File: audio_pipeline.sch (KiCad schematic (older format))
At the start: 8 parts, among them P1 CONN_4, P2 CONN_4, P3 CONN_4, P4 CONN_4, P5 CONN_4, U5 MAX4582, U6 DS1882, U8 RC4580

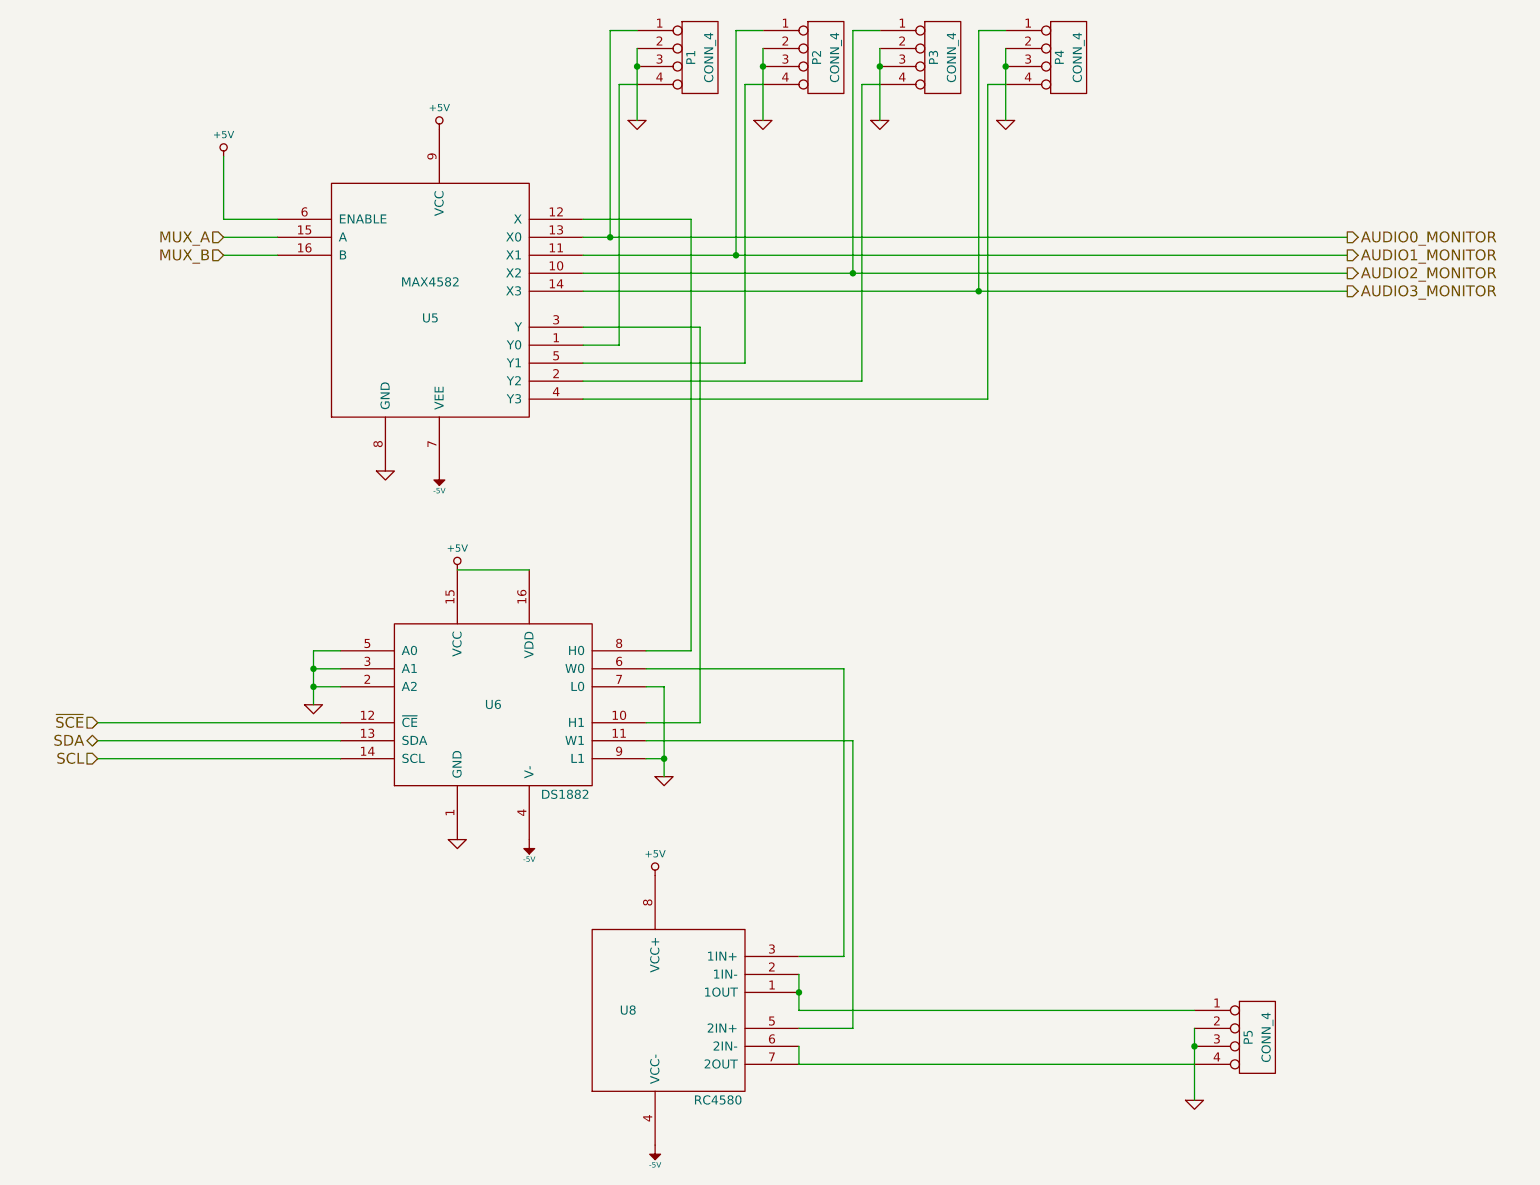
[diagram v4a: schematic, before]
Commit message: Moving back to atmega168, for cost and size reduction, new smaller board layout.
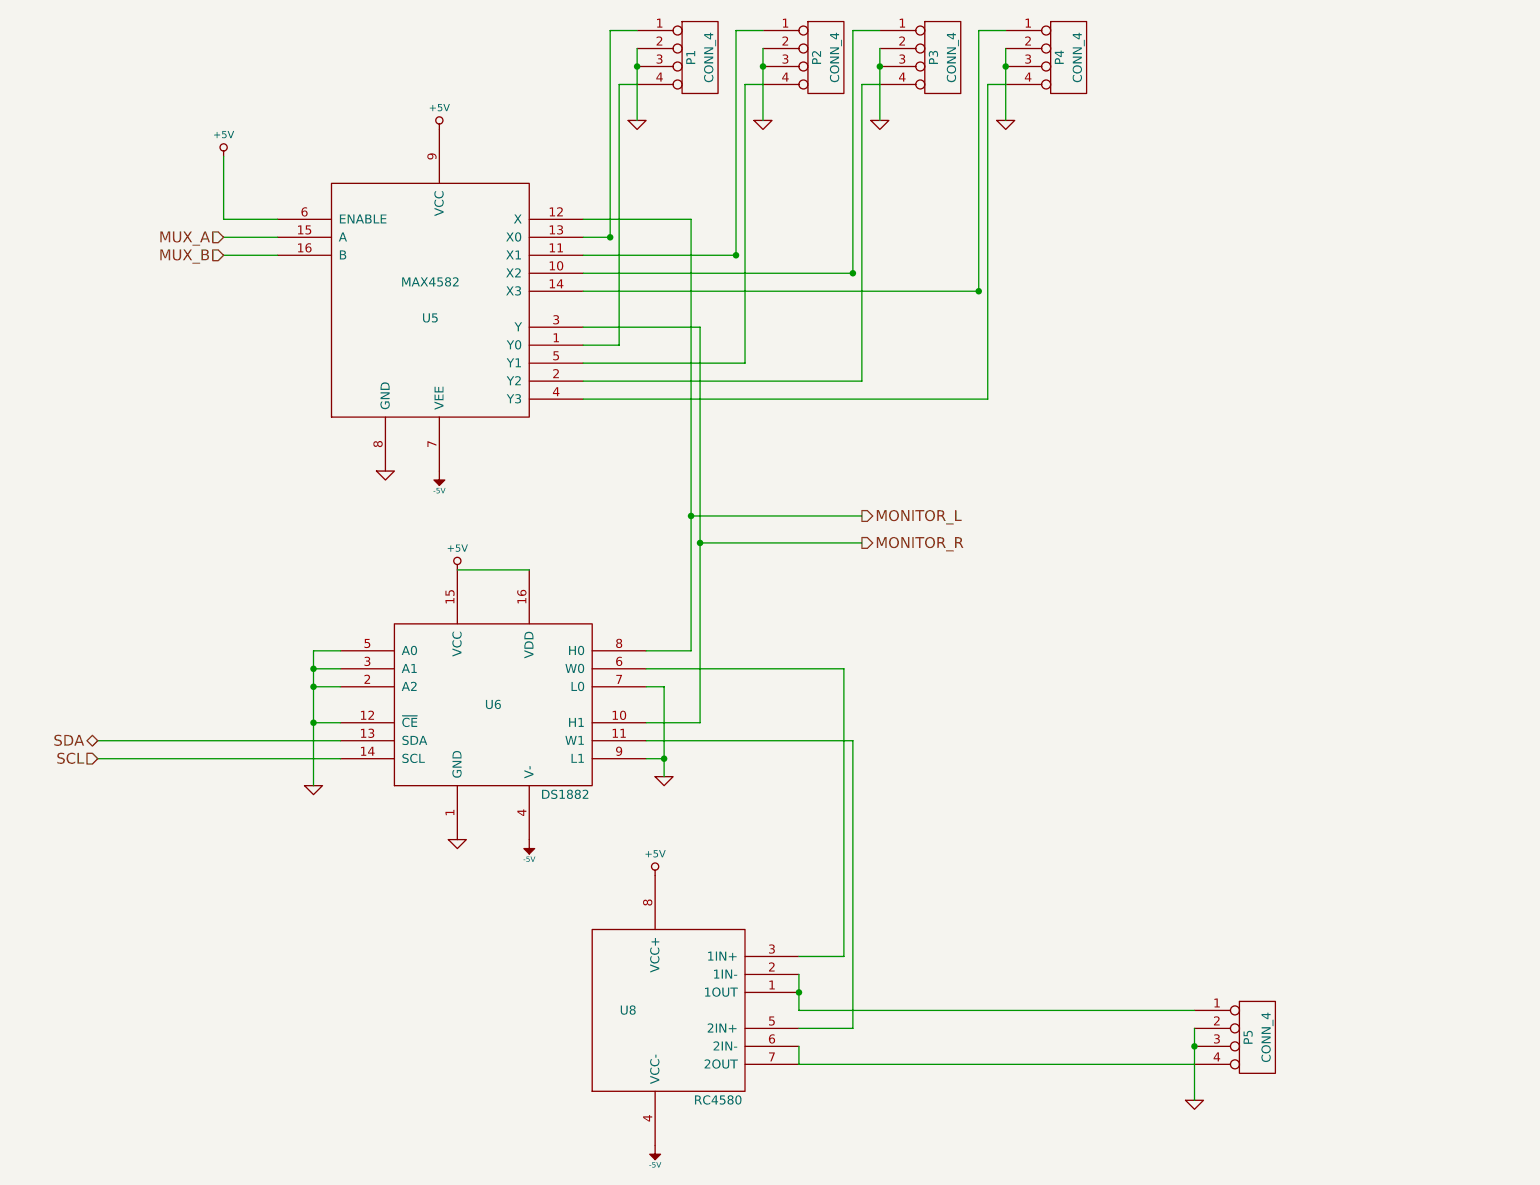
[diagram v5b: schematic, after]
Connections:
- net ~SCE is gone; now on net GND: U6.12 (~CE)
- net MONITOR_L: now reaches U5.12 (X), U6.8 (H0)
- net MONITOR_R: now reaches U5.3 (Y), U6.10 (H1)
- net AUDIO0_MONITOR: no longer names the net of P1.1 (P1), U5.13 (X0)
- net AUDIO1_MONITOR: no longer names the net of P2.1 (P1), U5.11 (X1)
- net AUDIO2_MONITOR: no longer names the net of P3.1 (P1), U5.10 (X2)
- net AUDIO3_MONITOR: no longer names the net of P4.1 (P1), U5.14 (X3)
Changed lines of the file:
@@
-EESchema Schematic File Version 2  date 7/31/2012 11:17:11 PM
+EESchema Schematic File Version 2  date 8/1/2012 10:20:13 AM
 LIBS:atmel
 LIBS:device
@@
 Comment4 ""
 $EndDescr
-Wire Wire Line
-	8400 2300 4150 2300
-Wire Wire Line
-	4150 2100 8400 2100
+Connection ~ 2650 4700
+Wire Wire Line
+	2800 4700 2650 4700
+Connection ~ 4800 3700
+Wire Wire Line
+	5700 3700 4800 3700
+Wire Wire Line
+	4150 2300 6350 2300
+Wire Wire Line
+	4150 2100 5000 2100
 Wire Wire Line
 	5350 6000 5600 6000
@@
 Connection ~ 4300 2000
 Wire Wire Line
-	4300 2000 4300 850
+	4300 850  4300 2000
 Wire Wire Line
 	4300 850  4450 850
@@
 	2800 4300 2650 4300
 Wire Wire Line
-	2650 4300 2650 4600
-Wire Wire Line
 	2800 4500 2650 4500
 Connection ~ 2650 4500
@@
 	2450 2000 2150 2000
 Wire Wire Line
-	2800 4700 1450 4700
-Wire Wire Line
 	4450 1150 4350 1150
 Wire Wire Line
@@
 	5650 6400 5350 6400
 Wire Wire Line
-	8400 2000 4150 2000
-Wire Wire Line
-	8400 2200 4150 2200
+	4300 2000 4150 2000
+Wire Wire Line
+	5650 2200 4150 2200
+Wire Wire Line
+	5700 3550 4750 3550
+Connection ~ 4750 3550
+Wire Wire Line
+	2650 4300 2650 5050
+Text HLabel 5700 3700 2    60   Output ~ 0
+MONITOR_R
+Text HLabel 5700 3550 2    60   Output ~ 0
+MONITOR_L
 $Comp
 L -5V #PWR024
@@
 	1    0    0    -1
 $EndComp
-Text HLabel 1450 4700 0    60   Input ~ 0
-~SCE
-Text HLabel 8400 2000 2    60   Output ~ 0
-AUDIO0_MONITOR
-Text HLabel 8400 2100 2    60   Output ~ 0
-AUDIO1_MONITOR
-Text HLabel 8400 2200 2    60   Output ~ 0
-AUDIO2_MONITOR
-Text HLabel 8400 2300 2    60   Output ~ 0
-AUDIO3_MONITOR
 $Comp
 L GND #PWR031
@@
 L GND #PWR035
 U 1 1 4F8E0C00
-P 2650 4600
-F 0 "#PWR035" H 2650 4600 30  0001 C CNN
-F 1 "GND" H 2650 4530 30  0001 C CNN
-	1    2650 4600
-	1    0    0    -1
-$EndComp
+P 2650 5050
+F 0 "#PWR035" H 2650 5050 30  0001 C CNN
+F 1 "GND" H 2650 4980 30  0001 C CNN
+	1    2650 5050
+	1    0    0    -1
+$EndComp

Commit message: Final board as sent for fab.
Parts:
- added C4, C6, C7, C8, C9: 0.1u, symbol C
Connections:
- net +5V: now also C4.1, C6.1, C8.1
- net -5V: now also C7.2, C9.2
- net GND: now also C4.2, C6.2, C7.1, C8.2, C9.1
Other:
- moved on the sheet: U8
